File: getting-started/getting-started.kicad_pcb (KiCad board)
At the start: 2 copper layers, 40 x 40 mm, 3 parts

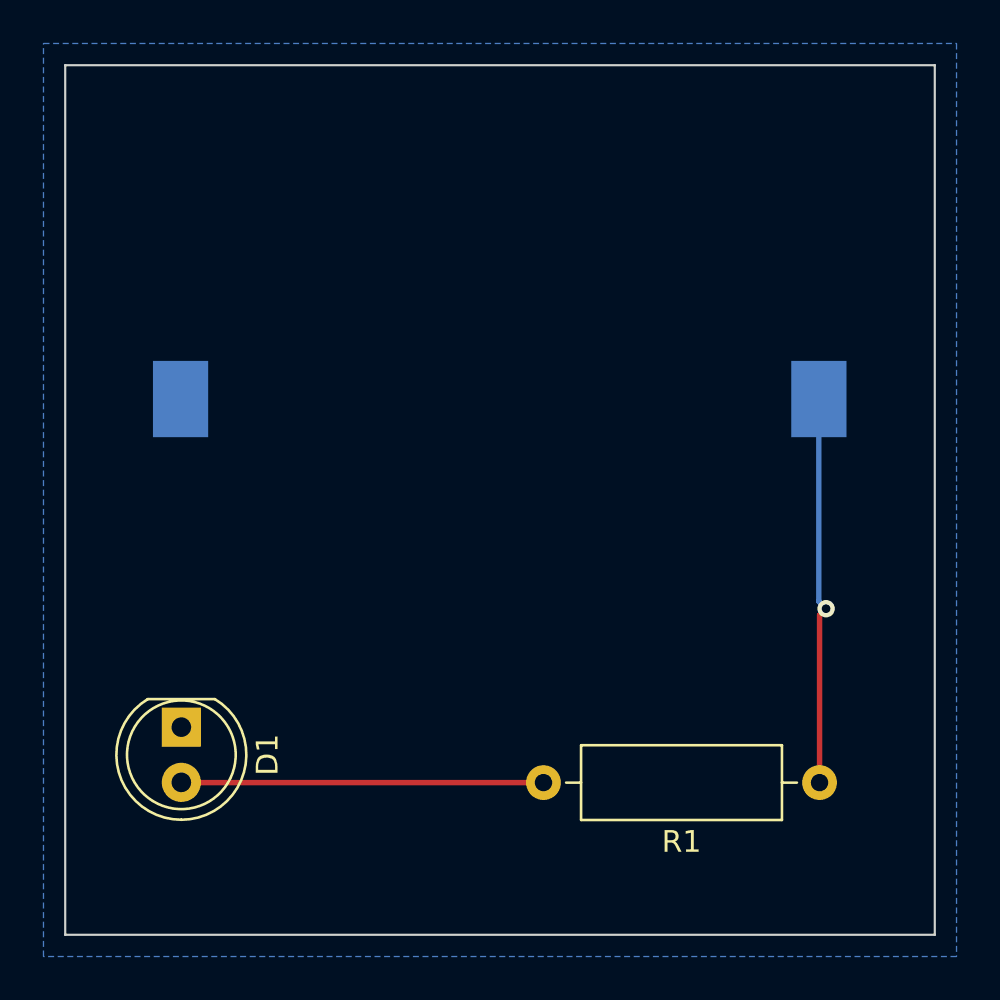
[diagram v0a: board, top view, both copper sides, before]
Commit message: Add new footprint to layout
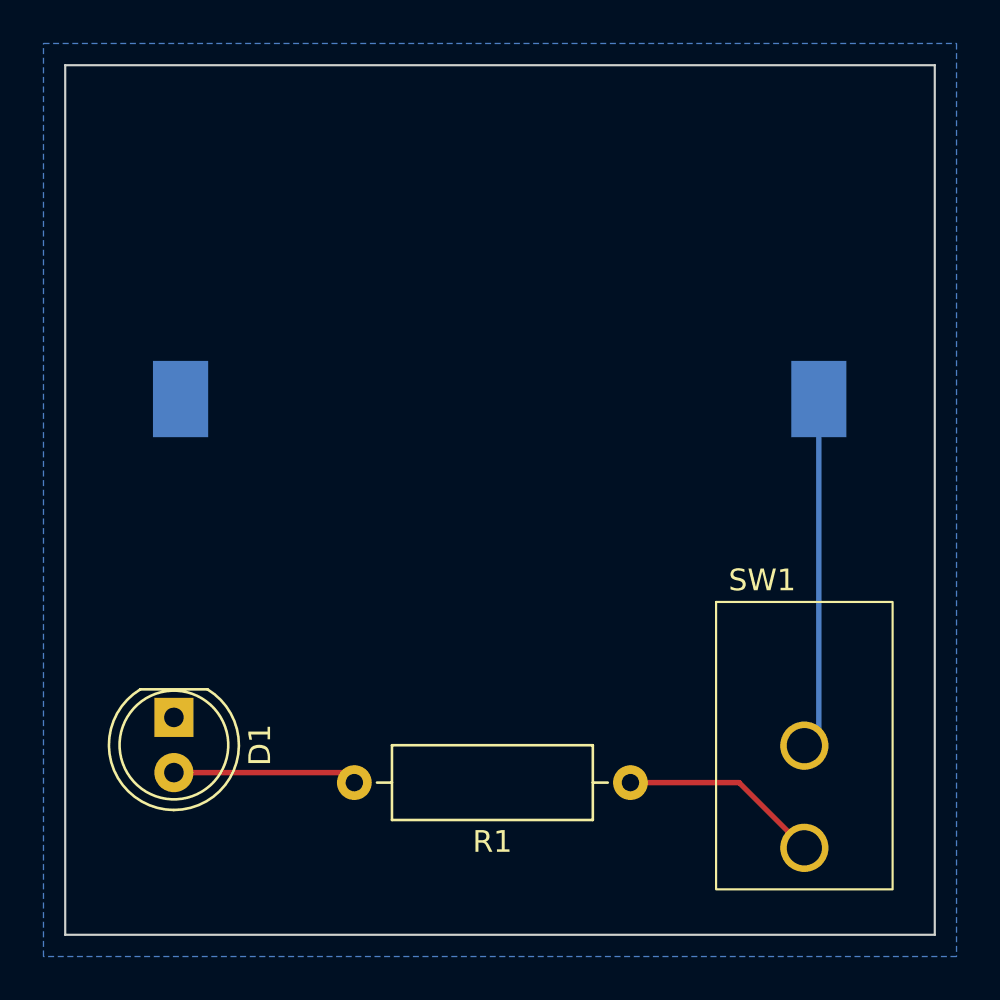
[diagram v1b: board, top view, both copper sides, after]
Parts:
- added SW1: M2011S3A1W03, getting-started:Switch_Toggle_SPST_NKK_M2011S3A1x03, F.Cu at (154.0, 116.6)
- moved R1 8.70 mm to (146.0, 123.0)
- moved D1 0.56 mm to (125.0, 120.0)
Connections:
- BT1 pad 1: VCC -> Net-(BT1-+)
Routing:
- net Net-(BT1-+): track 0.00 -> 16.2 mm
- net VCC: track 17.9 -> 9.24 mm, vias 1 -> 0
- net /led: track 16.7 -> 8.49 mm
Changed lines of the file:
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@@
   (net 2 "GND")
   (net 3 "/led")
+  (net 4 "Net-(BT1-+)")
   (footprint "LED_THT:LED_D5.0mm" (layer "F.Cu")
-    (at 125.342173 120.449143 -90)
+    (at 125 120 -90)
     (descr "LED, diameter 5.0mm, 2 pins, http://cdn-reichelt.de/documents/datenblatt/A500/LL-504BC2E-009.pdf")
     (tags "LED diameter 5.0mm 2 pins")
@@
   )
   (footprint "Resistor_THT:R_Axial_DIN0309_L9.0mm_D3.2mm_P12.70mm_Horizontal" (layer "F.Cu")
-    (at 154.7 123 180)
+    (at 146 123 180)
     (descr "Resistor, Axial_DIN0309 series, Axial, Horizontal, pin pitch=12.7mm, 0.5W = 1/2W, length*diameter=9*3.2mm^2, http://cdn-reichelt.de/documents/datenblatt/B400/1_4W%23YAG.pdf")
     (tags "Resistor Axial_DIN0309 series Axial Horizontal pin pitch 12.7mm 0.5W = 1/2W length 9mm diameter 3.2mm")
@@
     )
   )
+  (footprint "getting-started:Switch_Toggle_SPST_NKK_M2011S3A1x03" (layer "F.Cu")
+    (at 154 116.6)
+    (property "Sheetfile" "getting-started.kicad_sch")
+    (property "Sheetname" "")
+    (property "ki_keywords" "spst switch toggle")
+    (attr through_hole)
+    (fp_text reference "SW1" (at -1.94 -2.91 unlocked) (layer "F.SilkS")
+        (effects (font (size 1 1) (thickness 0.1)))
+    )
+    (fp_text value "M2011S3A1W03" (at 0 13.09 unlocked) (layer "F.Fab")
+        (effects (font (size 1 1) (thickness 0.15)))
+    )
+    (fp_text user "${REFERENCE}" (at 0 1.09 unlocked) (layer "F.Fab")
+        (effects (font (size 1 1) (thickness 0.15)))
+    )
+    (fp_rect (start -4.06 -1.91) (end 4.06 11.31)
+      (stroke (width 0.1) (type default)) (fill none) (layer "F.SilkS"))
+    (fp_rect (start -4.2 -2.05) (end 4.2 11.45)
+      (stroke (width 0.05) (type default)) (fill none) (layer "F.CrtYd"))
+    (fp_rect (start -3.95 -1.8) (end 3.95 11.2)
+      (stroke (width 0.1) (type default)) (fill none) (layer "F.Fab"))
+    (pad "2" thru_hole circle (at 0 4.7) (size 2.22 2.22) (drill 1.62) (layers "*.Cu" "*.Mask")
+      (net 4 "Net-(BT1-+)") (pinfunction "A") (pintype "passive"))
+    (pad "3" thru_hole circle (at 0 9.4) (size 2.22 2.22) (drill 1.62) (layers "*.Cu" "*.Mask")
+      (net 1 "VCC") (pinfunction "B") (pintype "passive"))
+  )
   (footprint "Battery:BatteryHolder_Keystone_1058_1x2032" (layer "B.Cu")
     (at 139.985891 105.355936 180)
@@
       (stroke (width 0.1) (type solid)) (layer "B.Fab"))
     (pad "1" smd rect (at -14.68 0 180) (size 2.54 3.51) (layers "B.Cu" "B.Paste" "B.Mask")
-      (net 1 "VCC") (pinfunction "+") (pintype "passive"))
+      (net 4 "Net-(BT1-+)") (pinfunction "+") (pintype "passive"))
     (pad "2" smd rect (at 14.68 0 180) (size 2.54 3.51) (layers "B.Cu" "B.Paste" "B.Mask")
       (net 2 "GND") (pinfunction "-") (pintype "passive"))
@@
   (gr_rect (start 120 90) (end 160 130)
     (stroke (width 0.1) (type default)) (fill none) (layer "Edge.Cuts"))
-  (segment (start 154.7 115.3) (end 154.7 123) (width 0.25) (layer "F.Cu") (net 1))
-  (segment (start 155 115) (end 154.7 115.3) (width 0.25) (layer "F.Cu") (net 1))
-  (via (at 155 115) (size 0.8) (drill 0.4) (layers "F.Cu" "B.Cu") (net 1))
-  (segment (start 154.665891 114.665891) (end 155 115) (width 0.25) (layer "B.Cu") (net 1))
-  (segment (start 154.665891 105.355936) (end 154.665891 114.665891) (width 0.25) (layer "B.Cu") (net 1))
+  (segment (start 151 123) (end 154 126) (width 0.25) (layer "F.Cu") (net 1))
+  (segment (start 146 123) (end 151 123) (width 0.25) (layer "F.Cu") (net 1))
   (segment (start 125.305891 120.412861) (end 125.342173 120.449143) (width 0.25) (layer "B.Cu") (net 2))
-  (segment (start 125.35303 123) (end 125.342173 122.989143) (width 0.25) (layer "F.Cu") (net 3))
-  (segment (start 142 123) (end 125.35303 123) (width 0.25) (layer "F.Cu") (net 3))
+  (segment (start 125 122.54) (end 132.84 122.54) (width 0.25) (layer "F.Cu") (net 3))
+  (segment (start 132.84 122.54) (end 133.3 123) (width 0.25) (layer "F.Cu") (net 3))
+  (segment (start 154.665891 105.355936) (end 154.665891 120.634109) (width 0.25) (layer "B.Cu") (net 4))
+  (segment (start 154.665891 120.634109) (end 154 121.3) (width 0.25) (layer "B.Cu") (net 4))
   (zone (net 2) (net_name "GND") (layer "B.Cu") (hatch edge 0.5)
     (connect_pads (clearance 0.5))
